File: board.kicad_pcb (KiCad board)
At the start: 2 copper layers, 56 x 49.5 mm, 26 parts, among them J1 GB_Cart_Edge_32, U1 SST39SF040, U2 FM18W08, U3 74HC574, U4 74HC32, U5 74HC32, U6 74HC00

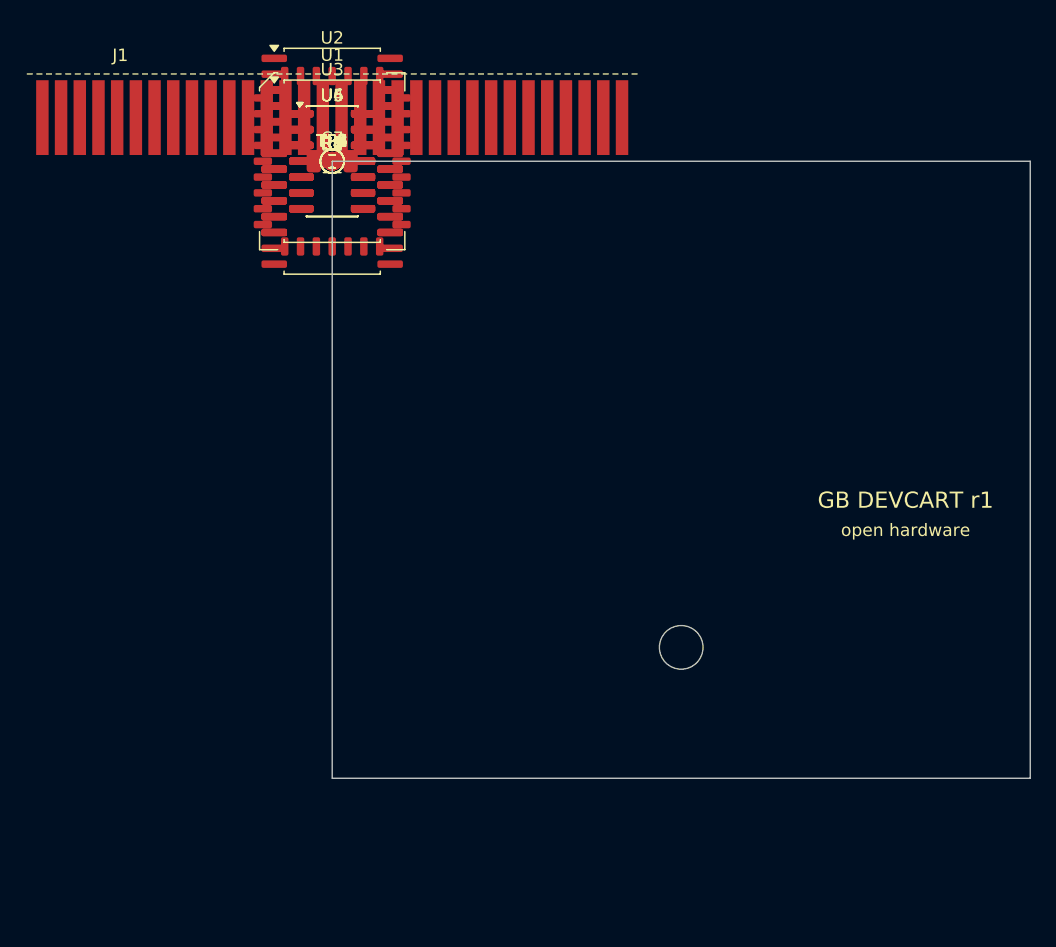
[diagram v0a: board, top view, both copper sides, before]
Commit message: Route the board with Freerouting; JLC part fields and order files
- Fully routed 2-layer board (134/134 connections) from fabdesk's route_run
  with Freerouting 2.4.1; DRC 0 errors / 0 unconnected, ERC clean. Placement
  tweaks (U2, U3, C2, C3, C6, R2-R6) and rules (0.2 mm track, 0.15 mm
  clearance, 0.5/0.3 mm vias) mirrored in circuit.netlist.json and gen.py.
- MPN / Manufacturer / LCSC on all 19 assembled parts in the board and
  schematic (scripts/sync_fields.py).
- exports/jlcpcb: gerbers.zip, bom.csv, cpl.csv (scripts/jlc_export.py).
- Refreshed GLB/STEP exports, 3D and routing renders, README status.

Co-Authored-By: Claude Opus 5.5 <noreply@anthropic.com>
Claude-Session: https://claude.ai/code/session_01K74FFAntk76NicGJzRejN5
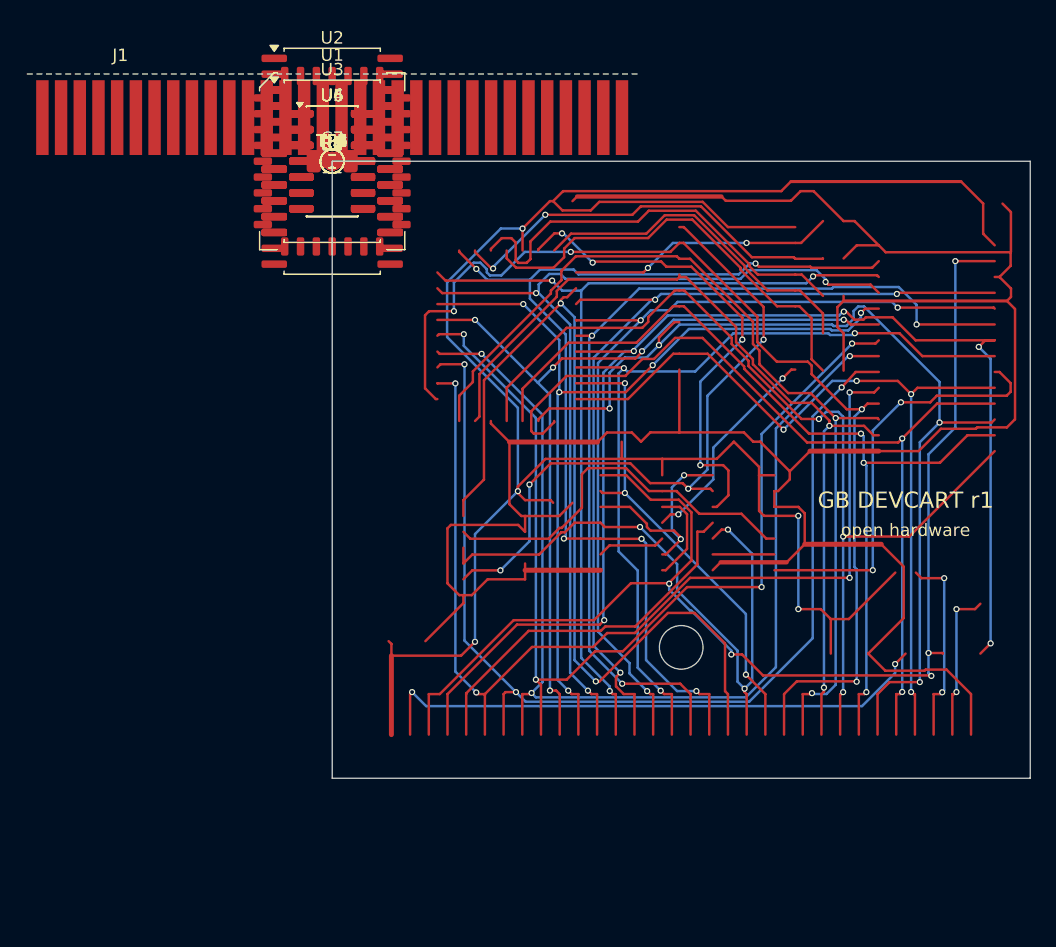
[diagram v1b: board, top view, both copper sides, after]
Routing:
- net GND: track 0.00 -> 220.8 mm
- net VCC: track 0.00 -> 176.8 mm, vias 0 -> 5
- net WR_N: track 0.00 -> 104.4 mm, vias 0 -> 5
- net RD_N: track 0.00 -> 104.3 mm, vias 0 -> 5
- net A2: track 0.00 -> 87.8 mm, vias 0 -> 3
- net D0: track 0.00 -> 87.3 mm, vias 0 -> 4
- net A1: track 0.00 -> 85.4 mm, vias 0 -> 3
- net A12: track 0.00 -> 83.5 mm, vias 0 -> 5
- net A3: track 0.00 -> 82.8 mm, vias 0 -> 4
- net A0: track 0.00 -> 81.4 mm, vias 0 -> 4
- net D5: track 0.00 -> 79.8 mm, vias 0 -> 4
- net D3: track 0.00 -> 79.0 mm, vias 0 -> 3
- net D1: track 0.00 -> 76.2 mm, vias 0 -> 2
- net A6: track 0.00 -> 75.6 mm, vias 0 -> 3
- net A11: track 0.00 -> 75.6 mm, vias 0 -> 3
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
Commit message: r1.1: DMG cartridge outline, re-routed, DRC clean
r1 (56 x 49.5 mm) did not fit a cartridge shell. r1.1 is the same circuit on
the OEM outline (51.4 x 61 mm, finger tongue, lock notch, shell holes),
1.0 mm thick, edge fingers 1.5 mm above the board edge.

- Re-placed inside the shell component zone and re-routed in fabdesk with
  Freerouting (134/134), copper keep-outs around both shell holes
- DRC 0 errors / 0 unconnected (silkscreen warnings only); fit check passes
  (PLCC-32 height warning)
- JLC gerbers / CPL, renders and README updated

Co-Authored-By: Claude Opus 5.5 <noreply@anthropic.com>
Claude-Session: https://claude.ai/code/session_01K74FFAntk76NicGJzRejN5
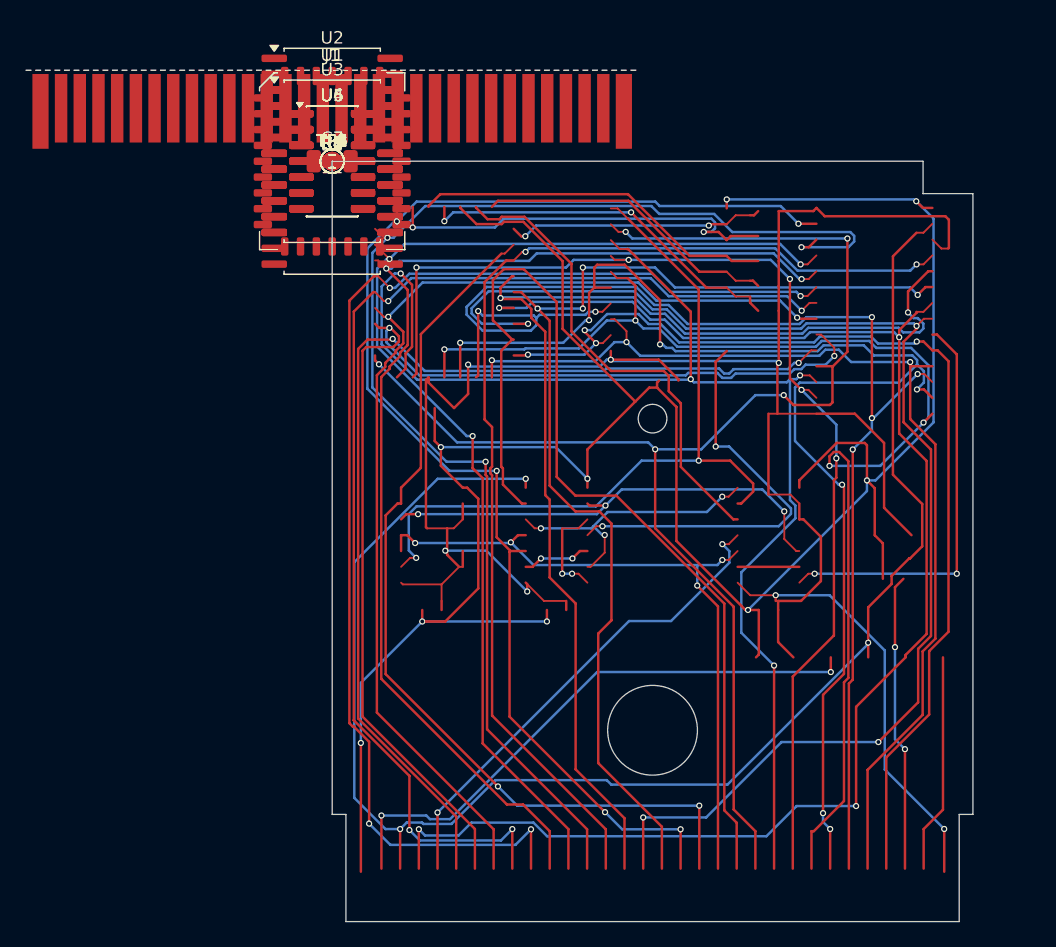
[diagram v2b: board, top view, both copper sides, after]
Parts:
- J1: footprint gbdev:GB_Cart_Edge_32 -> gbdev:GB_Cart_Edge_32_DMG
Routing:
- net A15: track 38.8 -> 80.0 mm, vias 3 -> 0
- net A10: track 67.6 -> 107.6 mm, vias 3 -> 4
- net D4: track 73.1 -> 107.4 mm, vias 3 -> 7
- net A7: track 73.5 -> 107.2 mm
- net D1: track 76.2 -> 109.0 mm, vias 2 -> 4
- net A4: track 69.0 -> 100.2 mm, vias 5 -> 4
- net D5: track 79.8 -> 110.5 mm, vias 4 -> 6
- net VCC: track 176.8 -> 205.5 mm, vias 5 -> 9
- net D0: track 87.3 -> 113.6 mm, vias 4 -> 5
- net GND: track 220.8 -> 194.8 mm, vias 0 -> 7
- net A9: track 71.1 -> 95.0 mm, vias 3 -> 2
- net WR_N: track 104.4 -> 127.5 mm, vias 5 -> 3
- net A12: track 83.5 -> 105.9 mm
- net D2: track 71.1 -> 93.1 mm, vias 2 -> 5
- net D3: track 79.0 -> 100.6 mm, vias 3 -> 4
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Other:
- board size 56 x 49.5 mm -> 51.4 x 61 mm
- board text removed: "GB DEVCART r1"
- board text removed: "open hardware"
